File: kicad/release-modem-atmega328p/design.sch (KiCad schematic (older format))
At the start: 23 parts, among them J1 ADC-Debug, J3 UART0, U3 ATmega328P-AU, Y1 AB308-16.000MHZ

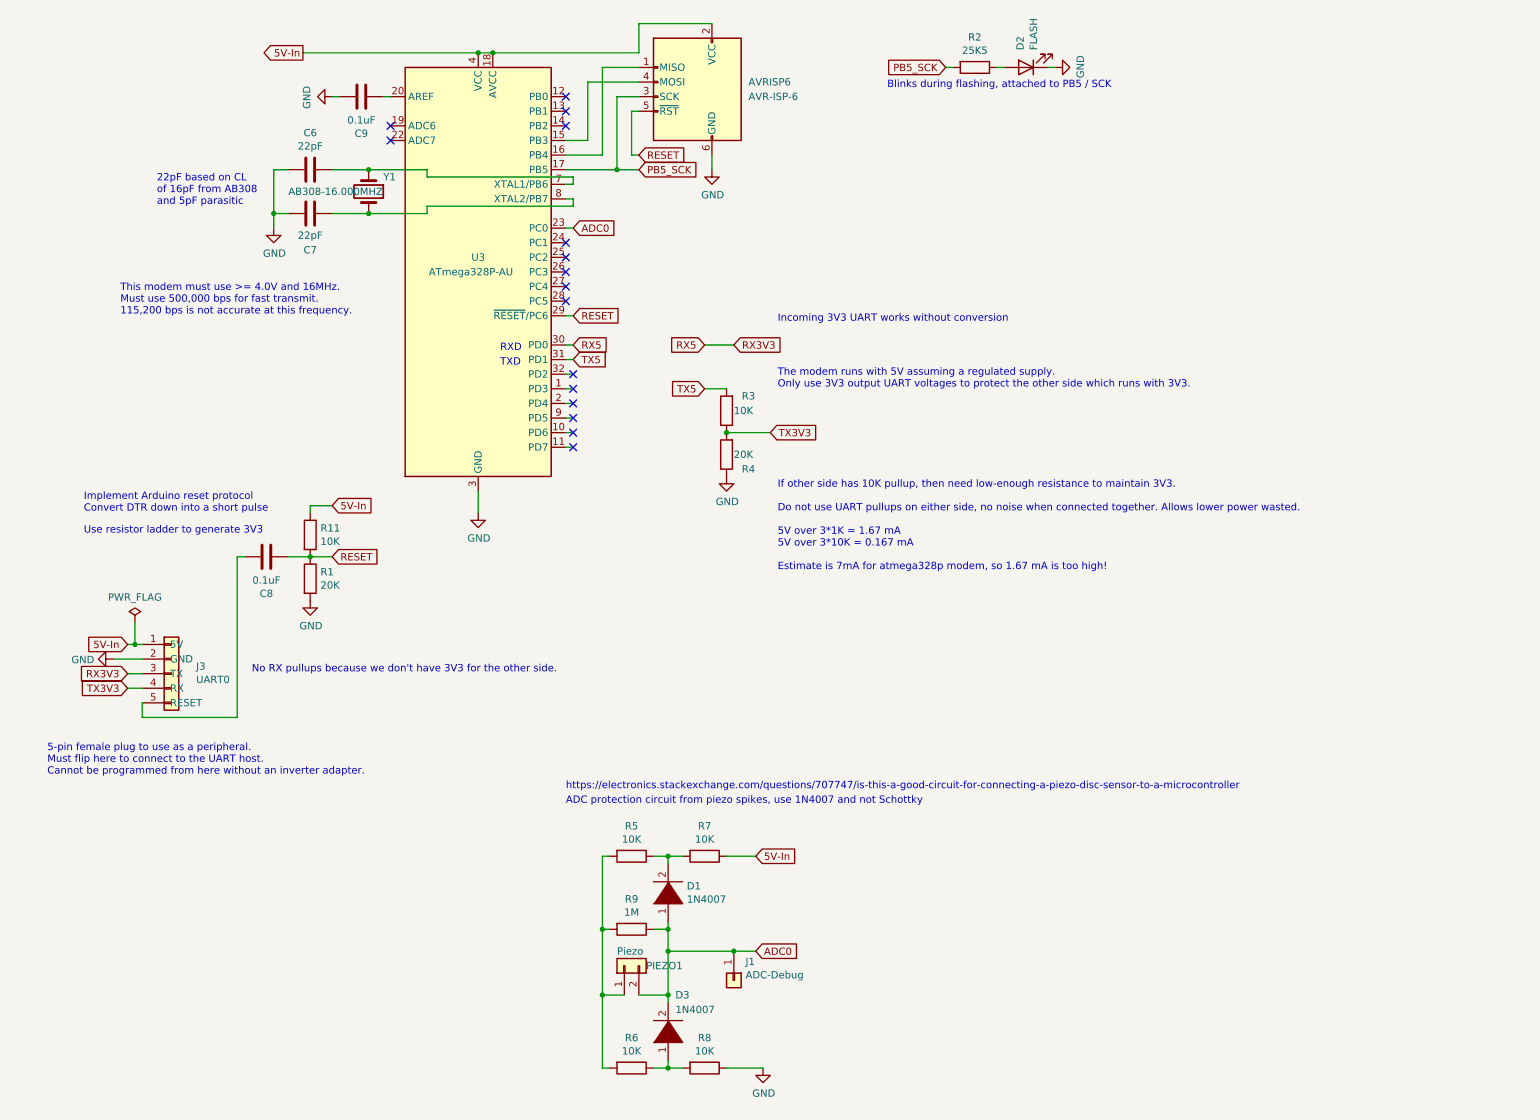
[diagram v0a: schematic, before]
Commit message: Rework the piezo input to use an OPA1641 opamp
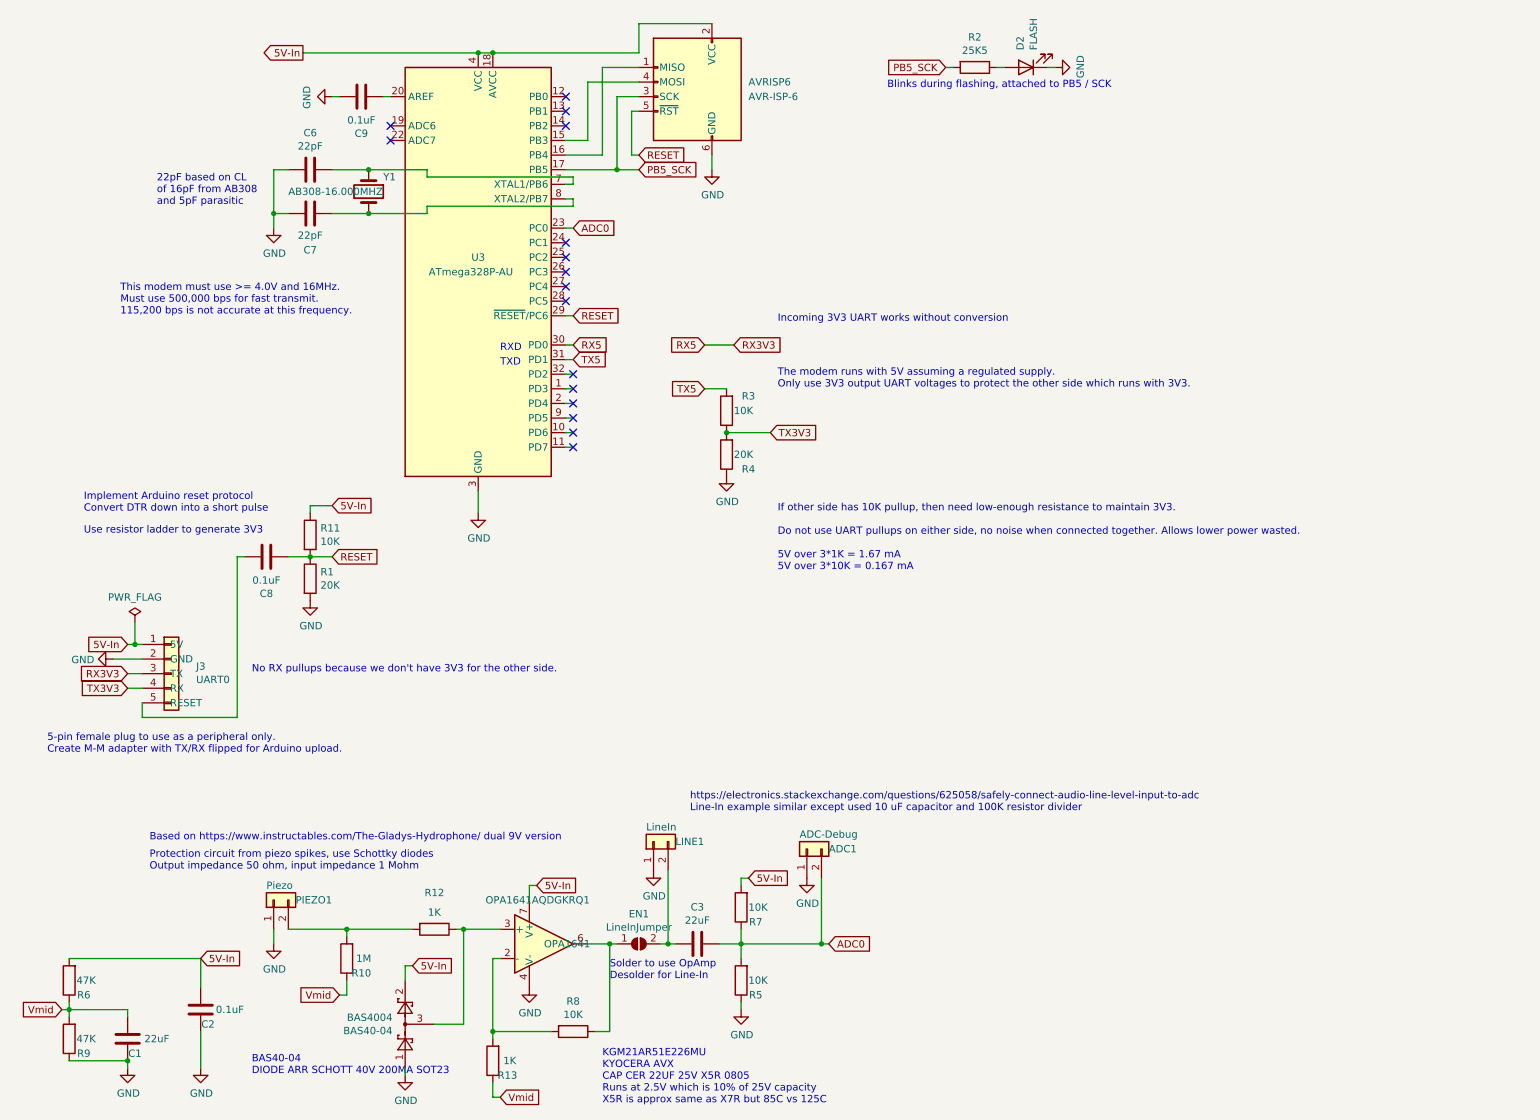
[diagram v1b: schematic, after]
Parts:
- removed D1, D3: 1N4007, custom:WP_D_SOD-123, symbol pspice:DIODE
- removed J1: ADC-Debug, Connector_PinHeader_2.54mm:PinHeader_1x01_P2.54mm_Vertical, symbol Connector_Generic:Conn_01x01
- added ADC1: ADC-Debug, custom:WP_PinSocket_1x02_P2.54mm_Vertical, symbol Connector_Generic:Conn_01x02
- added BAS4004: BAS40-04, Package_TO_SOT_SMD:SOT-23, symbol Diode:BAS40-04
- added C1, C3: 22uF, custom:WP_C_0805_2012Metric_Pad1.15x1.40mm_HandSolder, symbol Device:C
- added C2: 0.1uF, custom:WP_C_0805_2012Metric_Pad1.15x1.40mm_HandSolder, symbol Device:C
- added EN1: LineInJumper, Jumper:SolderJumper-2_P1.3mm_Open_Pad1.0x1.5mm, symbol Jumper:SolderJumper_2_Open
- added LINE1: LineIn, custom:WP_PinSocket_1x02_P2.54mm_Vertical, symbol Connector_Generic:Conn_01x02
- added OPA1641: OPA1641AQDGKRQ1, Package_SO:VSSOP-8_3.0x3.0mm_P0.65mm, symbol Amplifier_Operational:OPA1641
- added R10: 1M, custom:WP_R_0805_2012Metric_Pad1.15x1.40mm_HandSolder, symbol Device:R
- added R12, R13: 1K, custom:WP_R_0805_2012Metric_Pad1.15x1.40mm_HandSolder, symbol Device:R
- R6: value 10K -> 47K
- R9: value 1M -> 47K
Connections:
- net 5V-In: now also R6.2, R7.2, BAS4004.2, C2.2, OPA1641.7 (V+); no longer R7.1
- net ADC0: now also R5.2, R7.1, ADC1.2 (Pin_2), C3.1; no longer PIEZO1.2 (Pin_2), R9.1
- net GND: now also PIEZO1.1 (Pin_1), R5.1, R9.1, ADC1.1 (Pin_1), BAS4004.1, C1.1, C2.1, LINE1.1 (Pin_1), OPA1641.4 (V-); no longer R8.1
- net at R8.2: now also OPA1641.2 (-), R13.2; no longer R6.1
- new net: EN1.1 (A), OPA1641.6, R8.1
- new net: PIEZO1.2 (Pin_2), R10.2, R12.2
- new net: BAS4004.3, OPA1641.3 (+), R12.1
- new net: C3.2, EN1.2 (B), LINE1.2 (Pin_2)
- new net Vmid: C1.2, R10.1, R13.1, R6.1, R9.2
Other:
- note added: "5-pin female plug to use as a peripheral only.\nCreate M-M adapter with TX/RX flipped for Arduino upload."
- note added: "BAS40-04\nDIODE ARR SCHOTT 40V 200MA SOT23"
- note added: "Based on https://www.instructables.com/The-Gladys-Hydrophone/ dual 9V version"
- note added: "If other side has 10K pullup, then need low-enough resistance to maintain 3V3.\n\nDo not use UART pullups on either side, no noise when connected together. Allows lower power wasted.\n\n5V over 3*1K = 1.67 mA\n5V over 3*10K = 0.167 mA"
- note added: "KGM21AR51E226MU\nKYOCERA AVX\nCAP CER 22UF 25V X5R 0805\nRuns at 2.5V which is 10% of 25V capacity\nX5R is approx same as X7R but 85C vs 125C"
- note added: "Protection circuit from piezo spikes, use Schottky diodes\nOutput impedance 50 ohm, input impedance 1 Mohm"
- note added: "Solder to use OpAmp\nDesolder for Line-In"
- note added: "https://electronics.stackexchange.com/questions/625058/safely-connect-audio-line-level-input-to-adc\nLine-In example similar except used 10 uF capacitor and 100K resistor divider"
- note removed: "5-pin female plug to use as a peripheral.\nMust flip here to connect to the UART host.\nCannot be programmed from here without an inverter adapter."
- note removed: "ADC protection circuit from piezo spikes, use 1N4007 and not Schottky"
- note removed: "If other side has 10K pullup, then need low-enough resistance to maintain 3V3.\n\nDo not use UART pullups on either side, no noise when connected together. Allows lower power wasted.\n\n5V over 3*1K = 1.67 mA\n5V over 3*10K = 0.167 mA\n\nEstimate is 7mA for atmega328p modem, so 1.67 mA is too high!"
- note removed: "https://electronics.stackexchange.com/questions/707747/is-this-a-good-circuit-for-connecting-a-piezo-disc-sensor-to-a-microcontroller"
- moved on the sheet: PIEZO1, R5, R7, R8
